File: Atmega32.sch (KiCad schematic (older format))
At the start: 30 parts, among them J5 Conn_02x10_Odd_Even, SW2 SW_Push_Dual_x2, U2 FT232RL, U3 ATmega328P-AU, Y2 Crystal

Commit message: file: finished schematic
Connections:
- net D+: now also J5.17 (Pin_17); no longer C13.1, R9.1
- net D-: now also J5.19 (Pin_19); no longer C14.1, R10.1
- net WS2812B: now reaches U3.9 (PD5)
- net D_P: now reaches J5.18 (Pin_18)
- net D_P: now also C13.1, R9.1
- net D_N: now reaches J5.20 (Pin_20)
- net D_N: now also C14.1, R10.1
- no-connect marks 24 -> 19
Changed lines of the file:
@@
 XTAL2
 NoConn ~ 7100 5500
-NoConn ~ 7100 5300
 NoConn ~ 7100 4000
 NoConn ~ 7100 4100
@@
 Text Label 8750 5850 0    50   ~ 0
 GND
-NoConn ~ 9050 5950
-NoConn ~ 9050 6050
 Wire Wire Line
 	9550 5150 9850 5150
@@
 Wire Wire Line
 	1850 4450 1850 4550
-Text HLabel 1350 4000 0    50   Input ~ 0
+Text HLabel 8750 5950 0    50   Input ~ 0
 D+
-Text HLabel 1350 4100 0    50   Input ~ 0
+Text HLabel 8750 6050 0    50   Input ~ 0
 D-
 $Comp
@@
 Wire Wire Line
 	2300 5100 2400 5100
-NoConn ~ 9550 5950
-NoConn ~ 9550 6050
 $Comp
 L power:+5V #PWR0142
@@
 	0    -1   -1   0
 $EndComp
+Text Label 1350 4000 0    50   ~ 0
+D_P
+Text Label 1350 4100 0    50   ~ 0
+D_N
+Wire Wire Line
+	9550 5950 9850 5950
+Text Label 9850 5950 2    50   ~ 0
+D_P
+Text Label 9850 6050 2    50   ~ 0
+D_N
+Wire Wire Line
+	9550 6050 9850 6050
+Wire Wire Line
+	8750 5950 9050 5950
+Wire Wire Line
+	8750 6050 9050 6050
+Text HLabel 7400 5300 2    50   Output ~ 0
+WS2812B
+Wire Wire Line
+	7100 5300 7400 5300
 $EndSCHEMATC

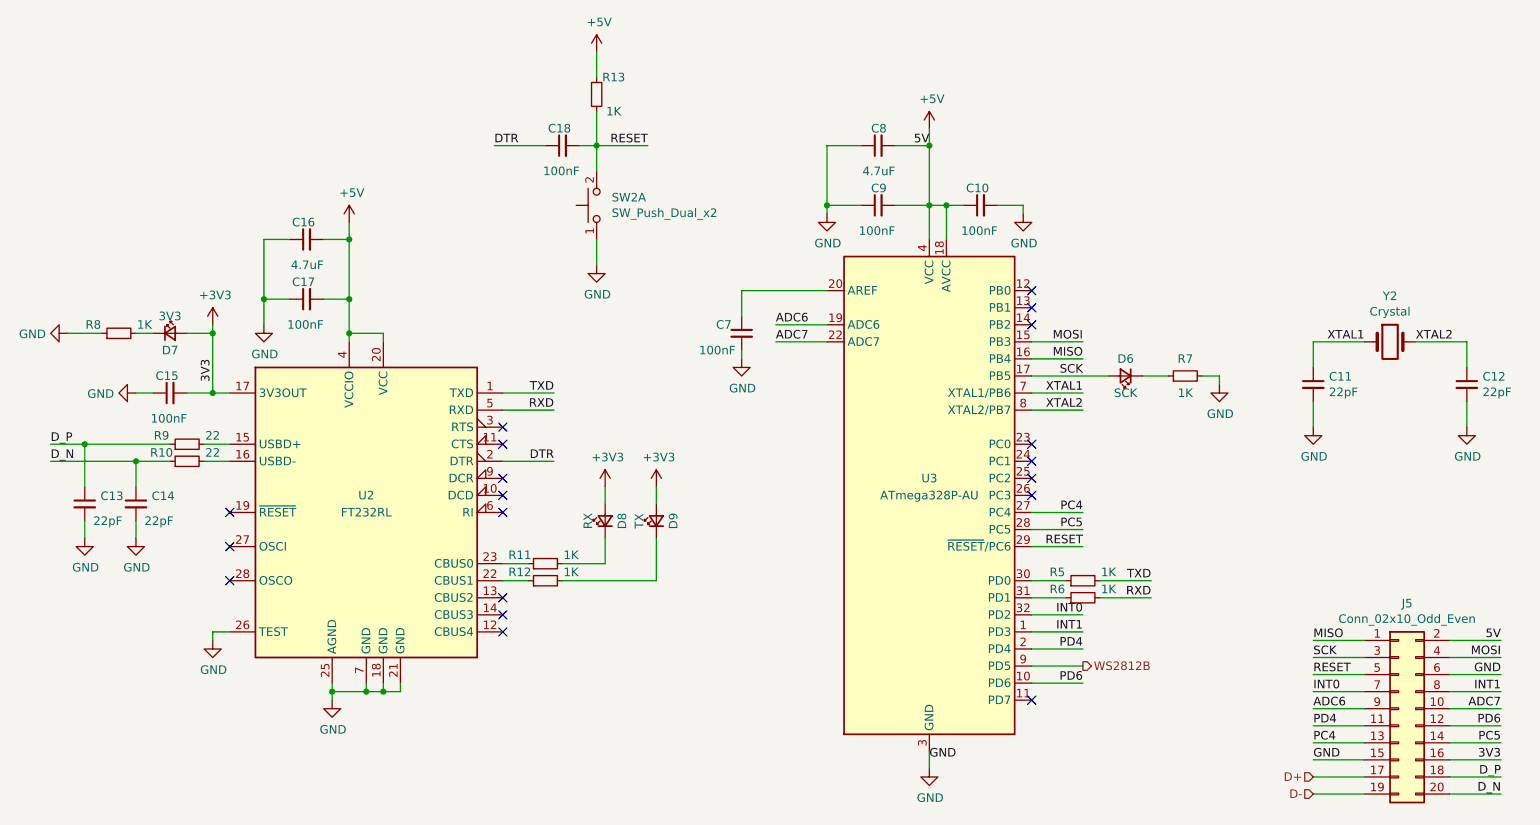
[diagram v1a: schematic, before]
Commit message: pcb schematic and layout edit i.e. finished -> orderd pcb jlcpcb
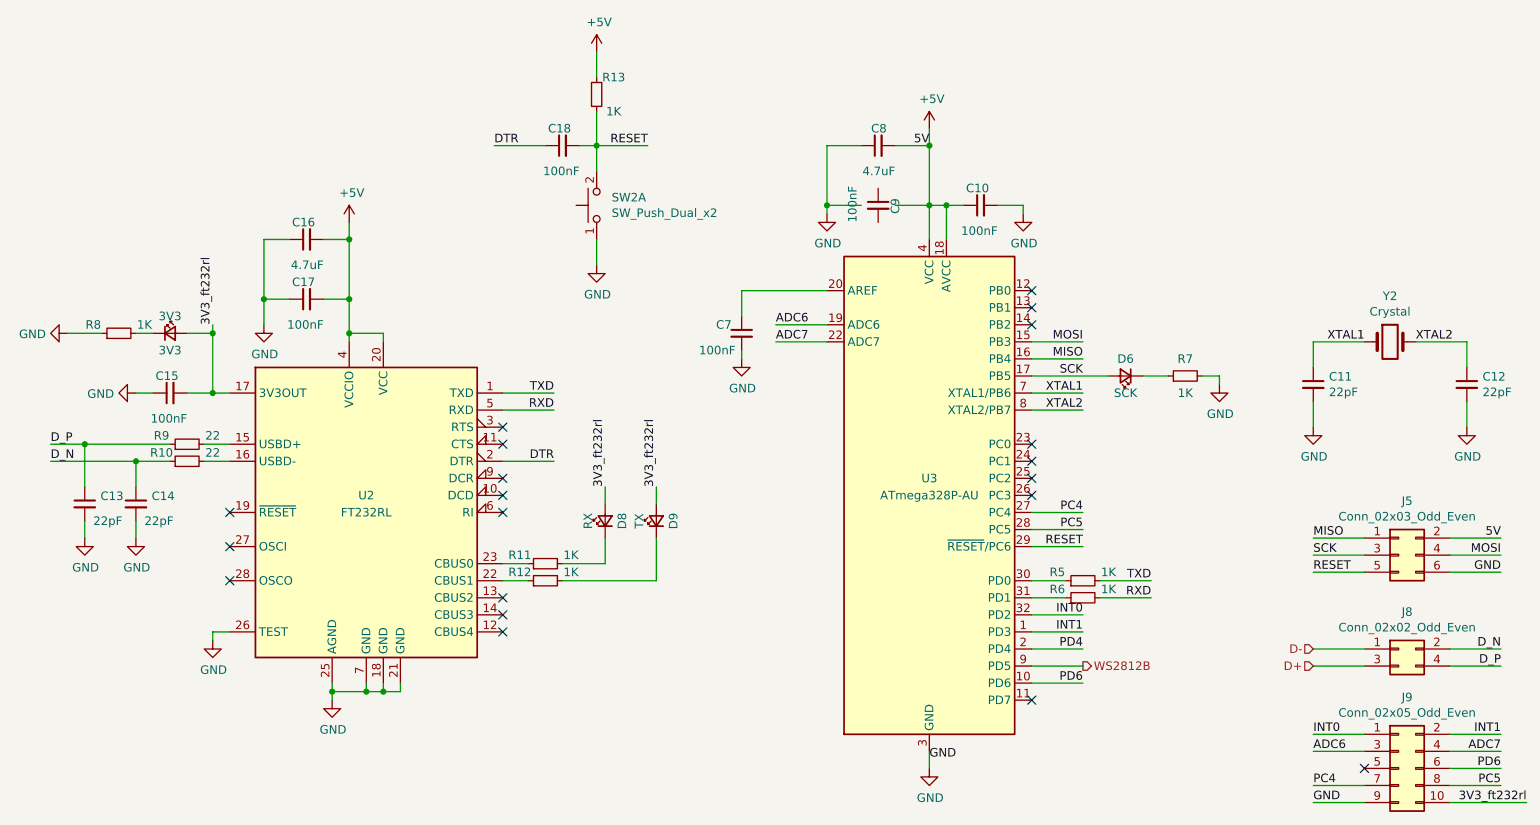
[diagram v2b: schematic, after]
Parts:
- removed J5: Conn_02x10_Odd_Even, Connector_PinHeader_2.00mm:PinHeader_2x10_P2.00mm_Vertical, symbol Connector_Generic:Conn_02x10_Odd_Even
- added J5: Conn_02x03_Odd_Even, Connector_PinHeader_2.00mm:PinHeader_2x03_P2.00mm_Vertical, symbol Connector_Generic:Conn_02x03_Odd_Even
- added J8: Conn_02x02_Odd_Even, Connector_PinHeader_2.00mm:PinHeader_2x02_P2.00mm_Vertical, symbol Connector_Generic:Conn_02x02_Odd_Even
- added J9: Conn_02x05_Odd_Even, Connector_PinHeader_2.00mm:PinHeader_2x05_P2.00mm_Vertical, symbol Connector_Generic:Conn_02x05_Odd_Even
- 3V3: renamed from D7; LCSC Part # (none) -> C72043
- C10, C15, C17, C18, C7, C9: LCSC Part # (none) -> C14663
- C11, C12, C13, C14: LCSC Part # (none) -> C1603
- C16, C8: LCSC Part # (none) -> C29823
- D6, D8, D9: LCSC Part # (none) -> C2286
- R10, R9: LCSC Part # (none) -> C23345
- R11, R12, R13, R5, R6, R7, R8: LCSC Part # (none) -> C21190
- U3: LCSC Part # (none) -> C14877
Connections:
- net +5V: now also J5.2 (Pin_2); no longer C9.2
- net ADC6: now also J9.3 (Pin_3)
- net ADC7: now also J9.4 (Pin_4)
- net D+: now also J8.3 (Pin_3)
- net D-: now also J8.1 (Pin_1)
- net D_N: now also J8.2 (Pin_2)
- net D_P: now also J8.4 (Pin_4)
- net GND: now also J5.6 (Pin_6), J9.9 (Pin_9); no longer C9.1
- net INT0: now also J9.1 (Pin_1)
- net INT1: now also J9.2 (Pin_2)
- net MISO: now also J5.1 (Pin_1)
- net MOSI: now also J5.4 (Pin_4)
- net PC4: now also J9.7 (Pin_7)
- net PC5: now also J9.8 (Pin_8)
- net PD6: now also J9.6 (Pin_6)
- net RESET: now also J5.5 (Pin_5)
- net SCK: now also J5.3 (Pin_3)
- net +3V3 renamed 3V3_ft232rl
- net 3V3_ft232rl: now also J9.10 (Pin_10)
- no-connect marks 19 -> 20
